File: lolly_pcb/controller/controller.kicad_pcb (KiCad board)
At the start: 2 copper layers, 94 x 94 mm, 6 parts, among them U1 ESP32-S2-MINI-1

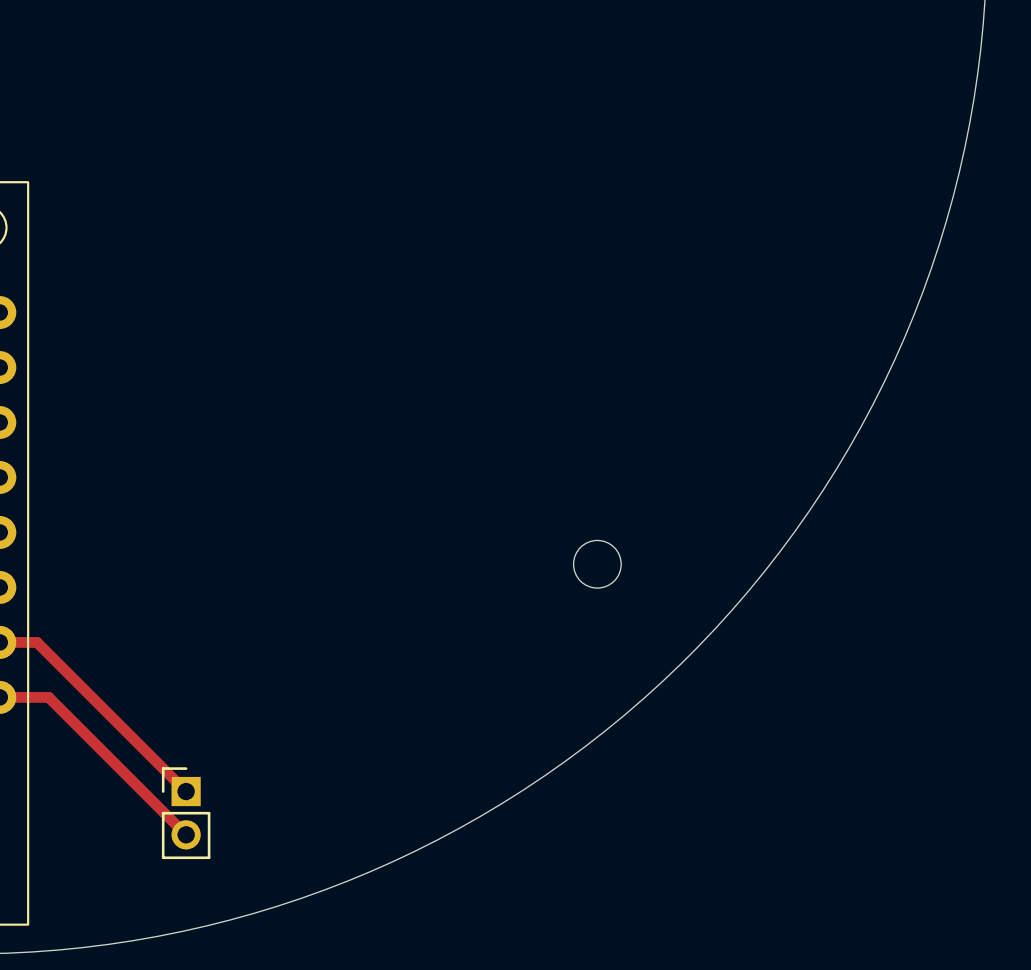
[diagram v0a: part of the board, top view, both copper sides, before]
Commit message: add charging circuit, connector and switch
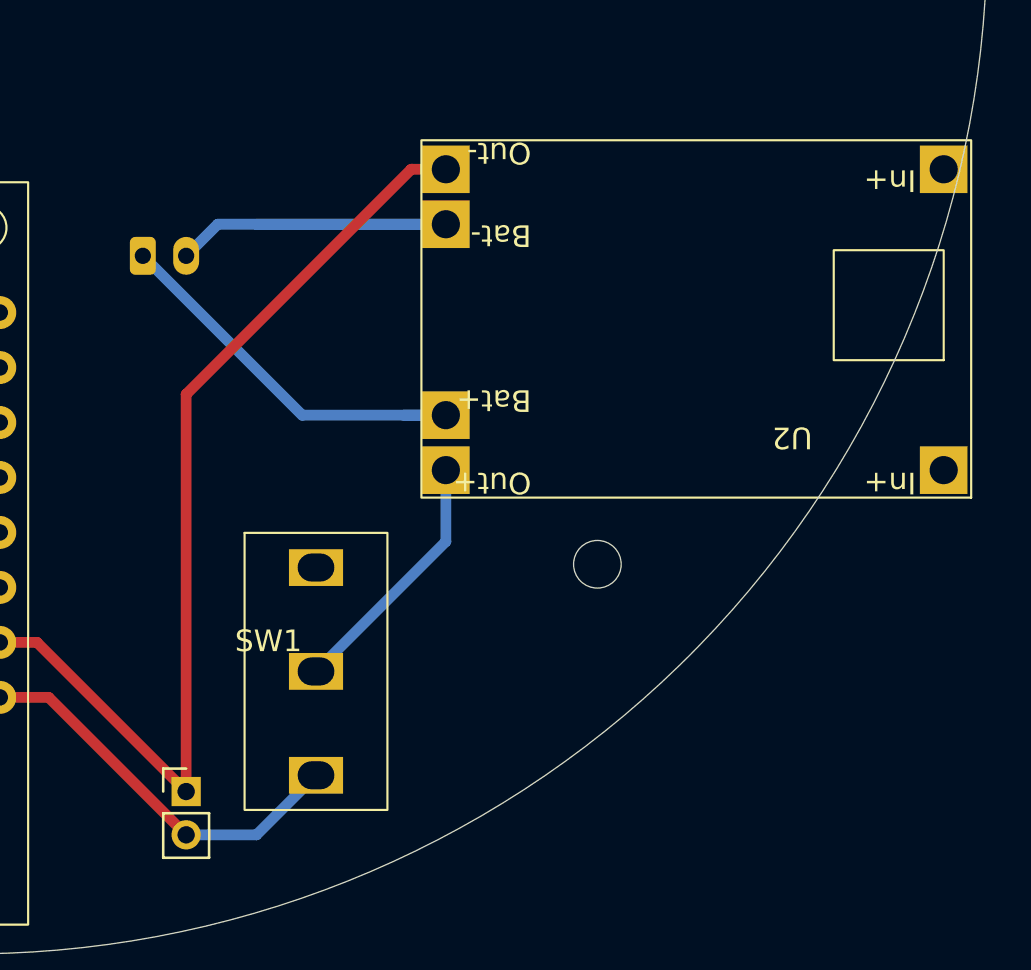
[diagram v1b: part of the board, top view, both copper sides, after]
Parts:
- added J1: Conn_01x02_Pin, Connector_JST:JST_PH_S2B-PH-K_1x02_P2.00mm_Horizontal, B.Cu at (158.0, 114.8)
- added SW1: SW_SPDT, controller:1P2T SPDT RUNCCI-YUN, F.Cu at (166.0, 133.9)
- added U2: ~, controller:tp4056 module, F.Cu at (195.0, 124.7)
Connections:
- U1 pad VBUS: VBUS -> (no net)
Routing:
- net GND: track 11.5 -> 46.1 mm
- net Bat-: track 0.00 -> 21.4 mm
- net Bat+: track 0.00 -> 19.0 mm
- net Net-(SW1-B): track 0.00 -> 11.8 mm
- net VBUS: track 11.2 -> 18.4 mm

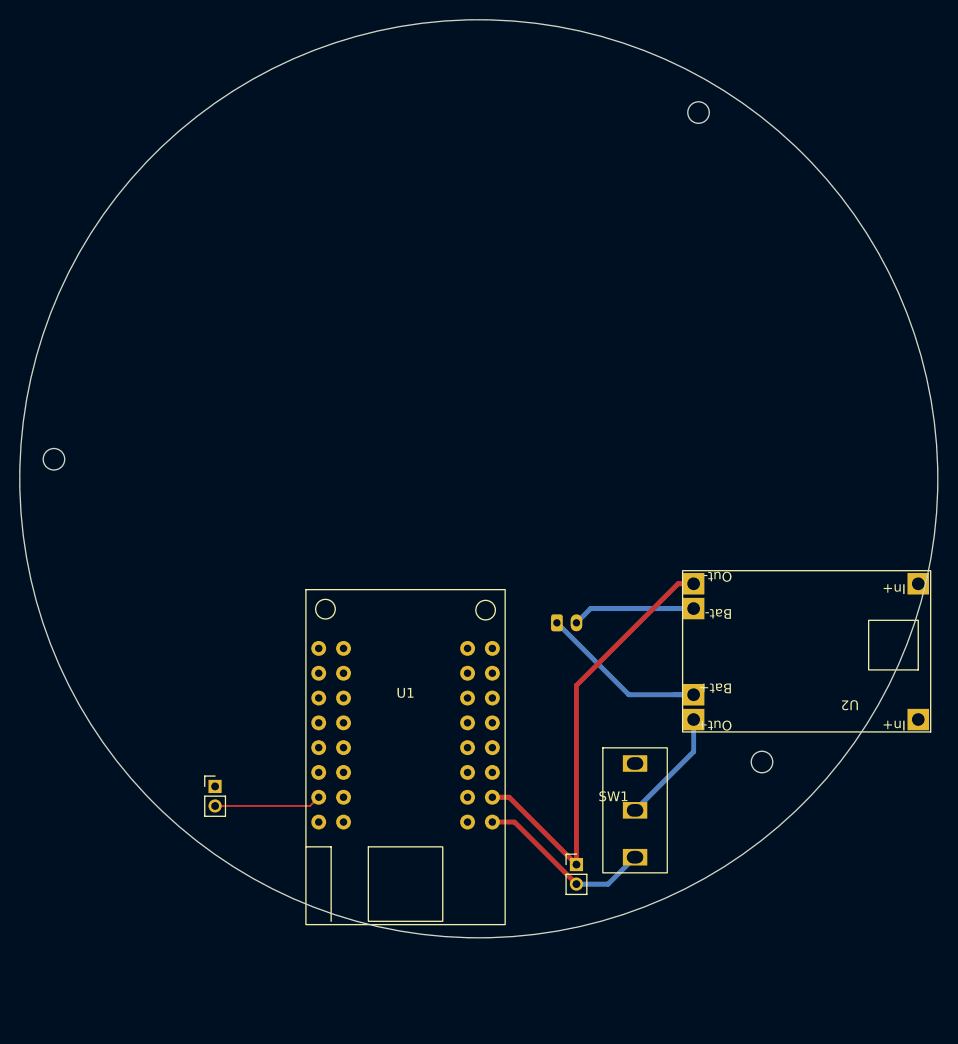
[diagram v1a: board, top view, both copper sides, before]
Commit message: first proper layout
includes solder pads for later components, better antenna placement, and routing
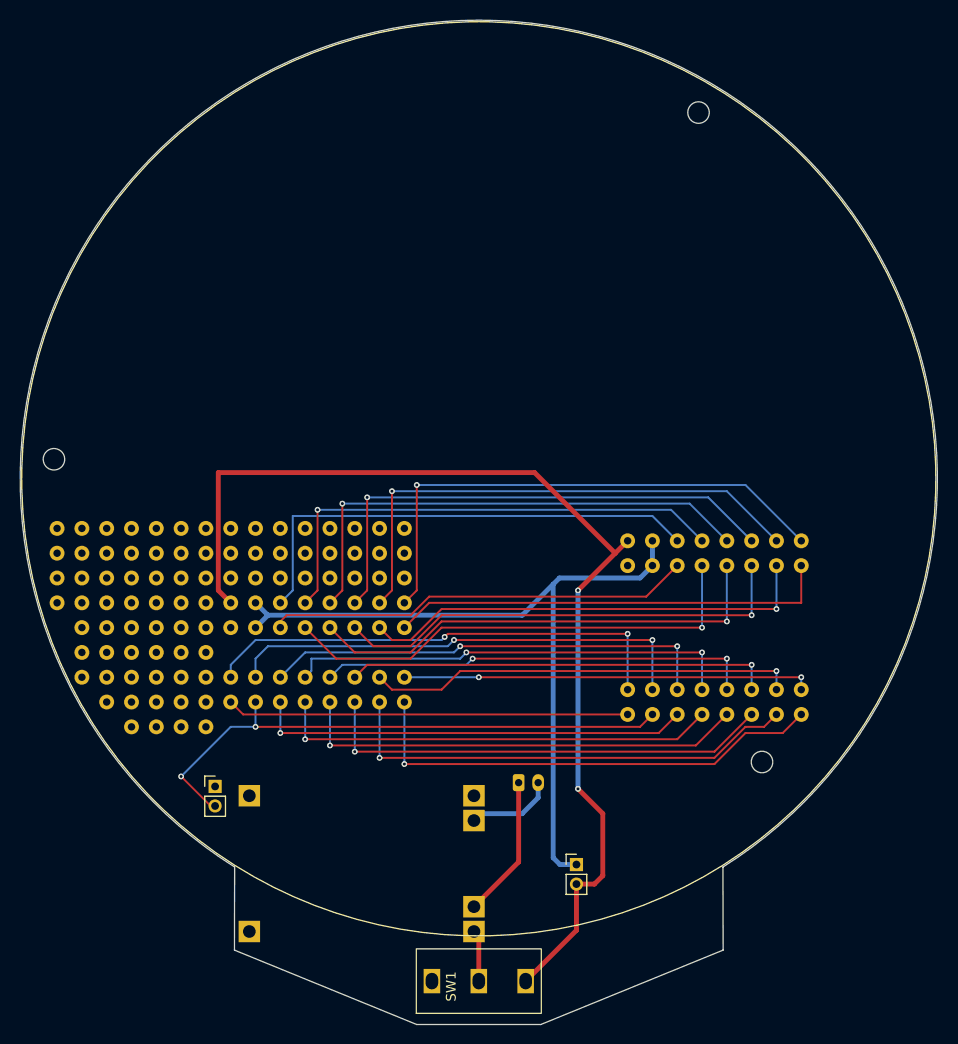
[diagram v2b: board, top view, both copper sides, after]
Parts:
- added ?: , , F.Cu at (124.6, 110.2)
- added ?: , , F.Cu at (122.1, 120.3)
- added ?: , , B.Cu at (127.1, 115.2)
- added ?: , , B.Cu at (129.7, 120.3)
- added ?: , , B.Cu at (134.8, 112.7)
- added ?: , , B.Cu at (127.1, 112.7)
- added ?: , , B.Cu at (139.8, 112.7)
- added ?: , , B.Cu at (142.4, 115.2)
- added ?: , , B.Cu at (129.7, 122.9)
- added ?: , , B.Cu at (139.8, 122.9)
- added ?: , , B.Cu at (129.7, 112.7)
- added ?: , , B.Cu at (142.4, 112.7)
- added ?: , , F.Cu at (106.8, 105.1)
- added ?: , , B.Cu at (137.3, 122.9)
- added ?: , , B.Cu at (132.2, 122.9)
- added ?: , , F.Cu at (122.1, 122.9)
- added ?: , , F.Cu at (117.0, 117.8)
- added ?: , , F.Cu at (124.6, 107.6)
- added ?: , , F.Cu at (114.4, 122.9)
- added ?: , , F.Cu at (111.9, 117.8)
- added ?: , , F.Cu at (119.5, 120.3)
- added ?: , , F.Cu at (132.2, 107.6)
- added ?: , , F.Cu at (117.0, 107.6)
- added ?: , , F.Cu at (122.1, 107.6)
- added ?: , , F.Cu at (137.3, 107.6)
- added ?: , , F.Cu at (129.7, 107.6)
- added ?: , , F.Cu at (129.7, 105.1)
- added ?: , , F.Cu at (109.4, 112.7)
- added ?: , , F.Cu at (111.9, 122.9)
- added ?: , , F.Cu at (127.1, 107.6)
- added ?: , , F.Cu at (109.4, 115.2)
- added ?: , , F.Cu at (111.9, 112.7)
- added ?: , , F.Cu at (127.1, 105.1)
- added ?: , , F.Cu at (119.5, 115.2)
- added ?: , , F.Cu at (124.6, 105.1)
- added ?: , , F.Cu at (117.0, 125.4)
- added ?: , , F.Cu at (139.8, 110.2)
- added ?: , , F.Cu at (122.1, 115.2)
- added ?: , , F.Cu at (127.1, 110.2)
- added ?: , , F.Cu at (122.1, 112.7)
- added ?: , , F.Cu at (122.1, 125.4)
- added ?: , , F.Cu at (134.8, 107.6)
- added ?: , , F.Cu at (109.4, 107.6)
- added ?: , , F.Cu at (129.7, 110.2)
- added ?: , , F.Cu at (117.0, 112.7)
- added ?: , , F.Cu at (109.4, 117.8)
- added ?: , , F.Cu at (139.8, 105.1)
- added ?: , , F.Cu at (114.4, 107.6)
- added ?: , , F.Cu at (114.4, 117.8)
- added ?: , , F.Cu at (119.5, 107.6)
- added ?: , , F.Cu at (142.4, 105.1)
- added ?: , , F.Cu at (114.4, 112.7)
- added ?: , , F.Cu at (119.5, 122.9)
- added ?: , , F.Cu at (137.3, 110.2)
- added ?: , , F.Cu at (109.4, 110.2)
- added ?: , , F.Cu at (119.5, 110.2)
- added ?: , , F.Cu at (119.5, 125.4)
- added ?: , , F.Cu at (106.8, 112.7)
- added ?: , , F.Cu at (132.2, 105.1)
- added ?: , , F.Cu at (109.4, 120.3)
- added ?: , , F.Cu at (114.4, 110.2)
- added ?: , , F.Cu at (142.4, 110.2)
- added ?: , , F.Cu at (117.0, 120.3)
- added ?: , , F.Cu at (117.0, 105.1)
- added ?: , , F.Cu at (119.5, 117.8)
- added ?: , , F.Cu at (142.4, 107.6)
- added ?: , , F.Cu at (139.8, 107.6)
- added ?: , , F.Cu at (117.0, 122.9)
- added ?: , , F.Cu at (106.8, 107.6)
- added ?: , , F.Cu at (119.5, 105.1)
- added ?: , , F.Cu at (119.5, 112.7)
- added ?: , , F.Cu at (114.4, 115.2)
- added ?: , , F.Cu at (111.9, 107.6)
- added ?: , , F.Cu at (111.9, 115.2)
- added ?: , , F.Cu at (117.0, 115.2)
- added ?: , , F.Cu at (114.4, 125.4)
- added ?: , , F.Cu at (134.8, 105.1)
- added ?: , , F.Cu at (111.9, 120.3)
- added ?: , , F.Cu at (106.8, 110.2)
- added ?: , , F.Cu at (109.4, 105.1)
- added ?: , , F.Cu at (137.3, 105.1)
- added ?: , , F.Cu at (122.1, 105.1)
- added ?: , , F.Cu at (134.8, 110.2)
- added ?: , , F.Cu at (132.2, 110.2)
- added ?: , , F.Cu at (117.0, 110.2)
- added ?: , , F.Cu at (114.4, 105.1)
- added ?: , , F.Cu at (111.9, 105.1)
- added ?: , , F.Cu at (122.1, 117.8)
- added ?: , , F.Cu at (114.4, 120.3)
- added ?: , , F.Cu at (111.9, 110.2)
- added ?: , , B.Cu at (134.8, 122.9)
- added ?: , , B.Cu at (132.2, 120.3)
- added ?: , , B.Cu at (124.6, 122.9)
- added ?: , , B.Cu at (132.2, 115.2)
- added ?: , , B.Cu at (132.2, 112.7)
- added ?: , , B.Cu at (124.6, 120.3)
- added ?: , , B.Cu at (124.6, 115.2)
- added ?: , , B.Cu at (142.4, 122.9)
- added ?: , , B.Cu at (124.6, 112.7)
- added ?: , , B.Cu at (137.3, 120.3)
- added ?: , , F.Cu at (122.1, 110.2)
- added ?: , , B.Cu at (142.4, 120.3)
- added ?: , , B.Cu at (137.3, 112.7)
- added ?: , , B.Cu at (134.8, 115.2)
- added ?: , , B.Cu at (127.1, 120.3)
- added ?: , , B.Cu at (129.7, 115.2)
- added ?: , , B.Cu at (137.3, 115.2)
- added ?: , , B.Cu at (139.8, 120.3)
- added ?: , , B.Cu at (139.8, 115.2)
- added ?: , , B.Cu at (134.8, 120.3)
- added ?: , , B.Cu at (127.1, 122.9)
- U1, U2: moved to B.Cu
- moved U2 71.9 mm to (126.5, 146.4), turned to 0 degrees
- moved U1 36.2 mm to (177.9, 115.2), turned to 90 degrees
- moved SW1 23.7 mm to (150.0, 151.4), turned to 90 degrees
- moved J1 16.8 mm to (154.1, 131.1)
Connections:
- U1 pad 17: (no net) -> 17
- U1 pad 18: (no net) -> 18
- U1 pad 21: 17 -> 21
- U1 pad VBUS: (no net) -> VBUS
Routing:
- net VBUS: track 18.4 -> 110.5 mm, vias 0 -> 2
- net 39: track 0.00 -> 54.3 mm, vias 0 -> 1
- net 37: track 0.00 -> 53.4 mm, vias 0 -> 1
- net 35: track 0.00 -> 52.5 mm, vias 0 -> 1
- net 33: track 0.00 -> 51.6 mm, vias 0 -> 1
- net 18: track 0.00 -> 50.7 mm, vias 0 -> 1
- net 16: track 0.00 -> 49.8 mm
- net 21: track 0.00 -> 49.6 mm, vias 0 -> 1
- net EN: track 0.00 -> 49.1 mm, vias 0 -> 1
- net 14: track 0.00 -> 48.9 mm, vias 0 -> 2
- net 34: track 0.00 -> 48.7 mm, vias 0 -> 1
- net 13: track 0.00 -> 48.4 mm, vias 0 -> 2
- net 3: track 0.00 -> 48.2 mm, vias 0 -> 1
- net 36: track 0.00 -> 47.8 mm, vias 0 -> 1
- net 5: track 0.00 -> 47.3 mm, vias 0 -> 1
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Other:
- board size 94 x 94 mm -> 93.9 x 102.8 mm
- board text added: "Bat -"
- board text added: "Bat+"

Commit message: better board outline
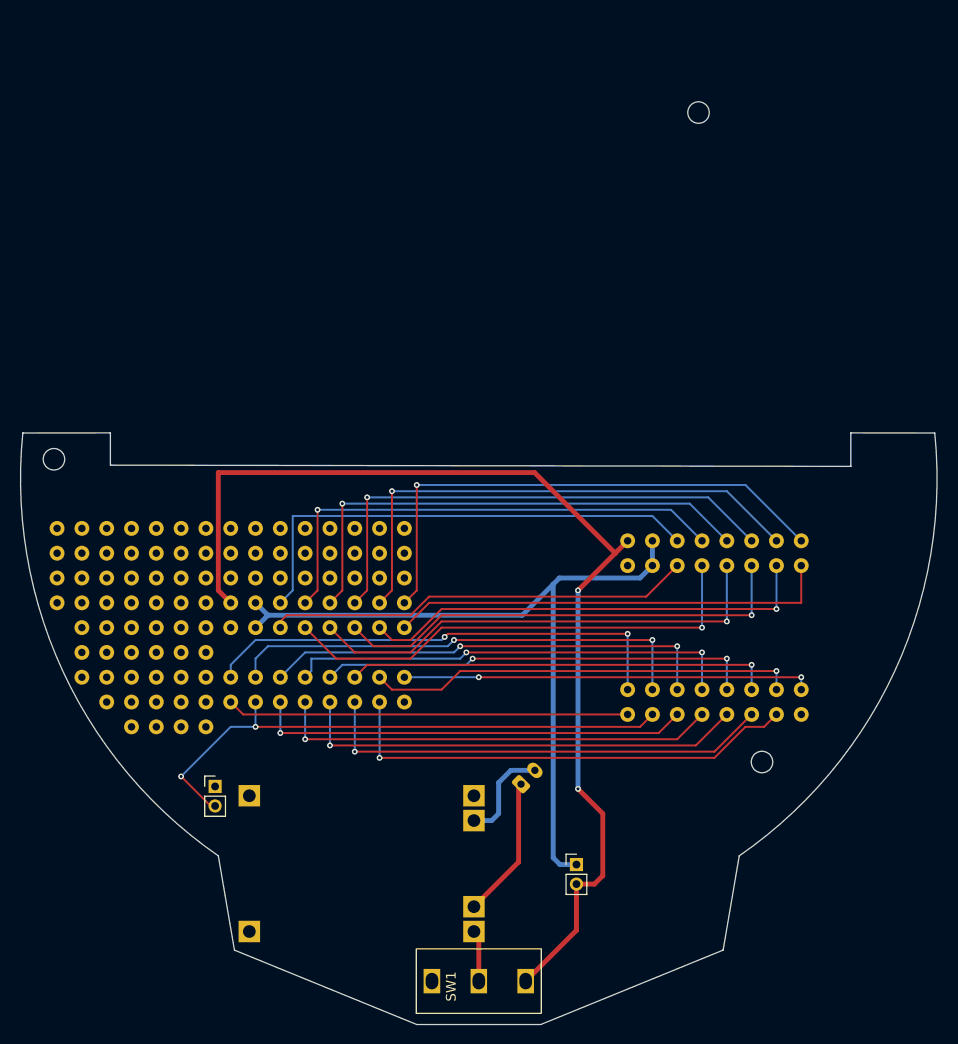
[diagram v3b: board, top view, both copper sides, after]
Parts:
- moved J1 0.29 mm to (154.3, 131.3), turned to 45 degrees
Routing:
- net EN: track 49.1 -> 0.00 mm, vias 1 -> 0
- net Bat-: track 9.08 -> 10.2 mm
- net Net-(SW1-B): track 5.29 -> 4.59 mm
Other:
- board size 93.9 x 102.8 mm -> 93.8 x 60.6 mm

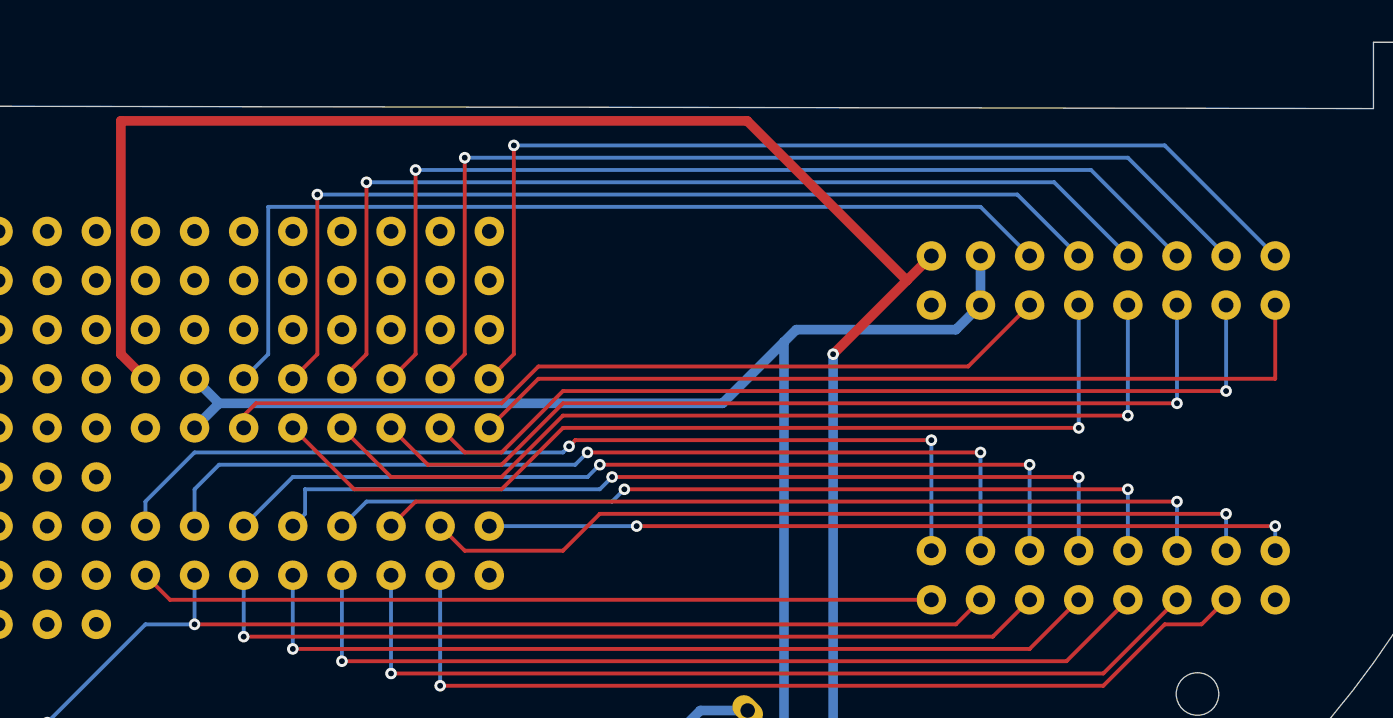
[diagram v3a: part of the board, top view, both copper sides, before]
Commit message: fix missing connection
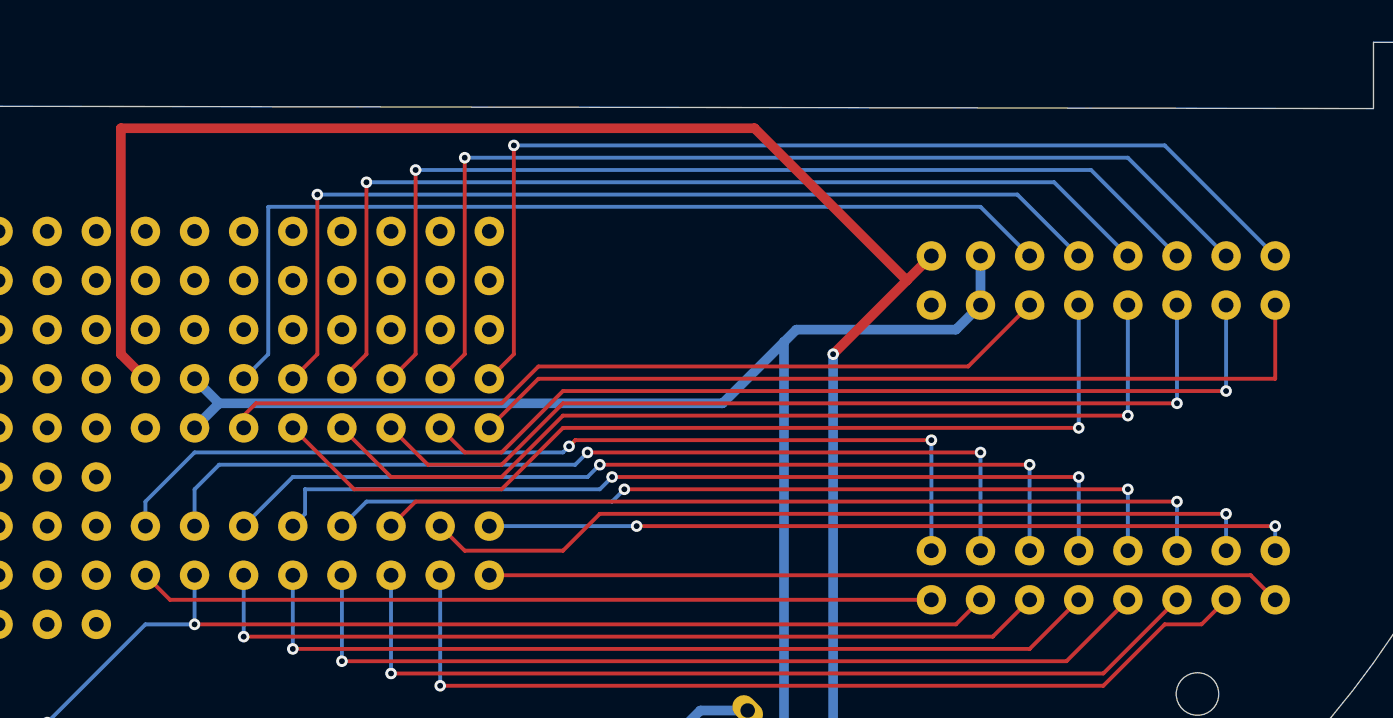
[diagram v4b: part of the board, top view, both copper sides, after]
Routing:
- net EN: track 0.00 -> 41.2 mm
- net VBUS: track 110.5 -> 110.0 mm
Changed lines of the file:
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@@
-	)
-	(gr_line
-		(start 188.1 95.301)
-		(end 196.688679 95.305982)
-		(stroke
-			(width 0.05)
-			(type default)
-		)
-		(layer "Edge.Cuts")
 	)
 	(gr_line
@@
 		(start 188.1 98.73)
 		(end 188.1 95.301)
+		(stroke
+			(width 0.05)
+			(type default)
+		)
+		(layer "Edge.Cuts")
+	)
+	(gr_line
+		(start 188.1 95.301)
+		(end 196.688679 95.305982)
 		(stroke
 			(width 0.05)
@@
 	)
 	(segment
+		(start 181.75 122.86)
+		(end 142.38 122.86)
+		(width 0.2)
+		(layer "F.Cu")
+		(net 26)
+	)
+	(segment
+		(start 183.02 124.13)
+		(end 181.75 122.86)
+		(width 0.2)
+		(layer "F.Cu")
+		(net 26)
+	)
+	(segment
 		(start 143.65 100.635)
 		(end 143.65 111.43)
@@
 	)
 	(segment
-		(start 155.715 99.365)
-		(end 123.33 99.365)
+		(start 123.33 99.746)
+		(end 123.33 111.43)
 		(width 0.5)
 		(layer "F.Cu")
@@
 	)
 	(segment
-		(start 123.33 99.365)
-		(end 123.33 111.43)
-		(width 0.5)
-		(layer "F.Cu")
-		(net 30)
-	)
-	(segment
 		(start 154.8 151.435)
 		(end 160 146.235)
@@
 	)
 	(segment
-		(start 163.97 107.62)
-		(end 155.715 99.365)
-		(width 0.5)
-		(layer "F.Cu")
-		(net 30)
-	)
-	(segment
 		(start 165.24 106.35)
 		(end 163.97 107.62)
@@
 	)
 	(segment
+		(start 156.096 99.746)
+		(end 123.33 99.746)
+		(width 0.5)
+		(layer "F.Cu")
+		(net 30)
+	)
+	(segment
 		(start 162.7 134.29)
 		(end 160.16 131.75)
 		(width 0.5)
 		(layer "F.Cu")
+		(net 30)
+	)
+	(segment
+		(start 163.97 107.62)
+		(end 156.096 99.746)
+		(width 0.5)
+		(layer "F.Cu")
